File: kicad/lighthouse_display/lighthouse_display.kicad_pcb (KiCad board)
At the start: 2 copper layers, 132 x 66.4 mm, 134 parts, among them J1 Conn_01x12_Pin, U1 IS31FL3731-SA, U2 TPS61176RTER

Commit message: use 7*6 white LEDs in a row now, almost all leds connected
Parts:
- removed D107: 1206MIL, LED_SMD:LED_1206_3216Metric_Pad1.42x1.75mm_HandSolder
- R4: value 83k3 -> 68k
- moved D102 90.9 mm to (87.0, 98.1)
- moved D101 73.1 mm to (87.0, 105.0)
- moved D106 66.0 mm to (171.0, 77.2)
- moved D103 50.1 mm to (123.0, 98.1)
- moved D88 41.8 mm to (147.0, 63.7)
- moved D95 30.3 mm to (135.0, 105.0)
- moved D90 30.2 mm to (147.0, 70.2)
- moved D98 30.2 mm to (153.0, 94.4)
- moved D104 27.7 mm to (123.0, 84.1)
- moved D86 25.0 mm to (123.0, 70.2)
- moved D81 24.9 mm to (123.0, 91.1)
- moved D76 24.8 mm to (105.0, 94.3)
- moved D77 24.1 mm to (99.0, 98.1)
- moved D93 24.0 mm to (135.0, 98.1)
- moved D87 23.9 mm to (123.0, 77.2)
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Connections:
- D101 pad 1: unconnected-(D101-K-Pad1) -> WHLED1
- D101 pad 2: unconnected-(D101-A-Pad2) -> Net-(D101-A)
- D102 pad 1: unconnected-(D102-K-Pad1) -> WHLED2
- D102 pad 2: unconnected-(D102-A-Pad2) -> Net-(D102-A)
- D103 pad 1: unconnected-(D103-K-Pad1) -> WHLED3
- D103 pad 2: unconnected-(D103-A-Pad2) -> Net-(D103-A)
- D104 pad 1: unconnected-(D104-K-Pad1) -> WHLED4
- D104 pad 2: unconnected-(D104-A-Pad2) -> Net-(D104-A)
- D105 pad 1: unconnected-(D105-K-Pad1) -> WHLED5
- D105 pad 2: unconnected-(D105-A-Pad2) -> Net-(D105-A)
- D106 pad 1: unconnected-(D106-K-Pad1) -> WHLED6
- D106 pad 2: unconnected-(D106-A-Pad2) -> Net-(D106-A)
- D69 pad 1: WHLED1 -> Net-(D101-A)
- D75 pad 1: WHLED2 -> Net-(D102-A)
- D81 pad 1: WHLED3 -> Net-(D103-A)
- D87 pad 1: WHLED4 -> Net-(D104-A)
- D98 pad 1: WHLED5 -> Net-(D105-A)
- D99 pad 1: WHLED6 -> Net-(D106-A)
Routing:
- net VLEDWH: track 0.00 -> 49.2 mm
- net Net-(D95-K): track 0.00 -> 34.5 mm
- net Net-(D77-K): track 0.00 -> 23.7 mm
- net Net-(D79-K): track 0.00 -> 22.0 mm
- net WHLED6: track 0.00 -> 18.4 mm
- net WHLED2: track 0.00 -> 17.4 mm
- net Net-(D101-A): track 0.00 -> 17.4 mm
- net Net-(D89-K): track 0.00 -> 16.2 mm
- net Net-(D67-K): track 0.00 -> 15.8 mm
- net WHLED3: track 0.00 -> 12.6 mm
- net WHLED1: track 0.00 -> 12.4 mm
- net Net-(D80-K): track 0.00 -> 12.1 mm
- net Net-(D97-K): track 0.00 -> 10.7 mm
- net WHLED5: track 0.00 -> 10.4 mm
- net Net-(D96-K): track 0.00 -> 9.33 mm
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
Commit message: 100% routed
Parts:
- moved JP1 49.6 mm to (128.0, 114.9), turned to 180 degrees
- moved JP2 48.5 mm to (104.4, 114.9), turned to 180 degrees
- moved C2 11.3 mm to (162.6, 111.2), turned to 90 degrees
- moved C1 9.20 mm to (164.3, 111.1), turned to 90 degrees
- moved R4 4.30 mm to (160.1, 106.2)
- moved C5 3.22 mm to (160.6, 109.1), turned to -90 degrees
- moved C8 1.43 mm to (59.4, 102.4), turned to 90 degrees
- moved D100 1.05 mm to (163.6, 108.0)
- moved R3 1.01 mm to (163.4, 106.2), turned to 0 degrees
- moved C7 0.83 mm to (57.5, 102.2), turned to 90 degrees
- moved R11 0.05 mm to (73.4, 110.1)
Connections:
- U2 pad 17: (no net) -> GND
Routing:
- net VLEDWH: track 49.2 -> 207.8 mm, vias 0 -> 7
- net /WHITE_PWM: track 0.00 -> 82.8 mm, vias 0 -> 5
- net WHLED1: track 12.4 -> 85.6 mm
- net WHLED2: track 17.4 -> 88.2 mm
- net /~{SDB}: track 3.36 -> 72.1 mm, vias 0 -> 2
- net /~{INTB}: track 1.90 -> 67.9 mm, vias 0 -> 2
- net +3.3V: track 9.66 -> 74.2 mm, vias 0 -> 2
- net /TPS_VIN: track 0.00 -> 59.4 mm
- net WHLED4: track 3.83 -> 60.6 mm, vias 0 -> 2
- net /IS_VIN: track 8.61 -> 64.5 mm
- net /SCL: track 4.04 -> 58.6 mm, vias 1 -> 4
- net /SDA: track 4.38 -> 58.6 mm, vias 1 -> 4
- net CB1: track 178.0 -> 224.9 mm, vias 5 -> 6
- net +12V: track 0.00 -> 46.9 mm
- net CB2: track 186.0 -> 232.7 mm, vias 5 -> 6
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- added copper zone on B.Cu, net GND
- added copper zone on F.Cu, net GND

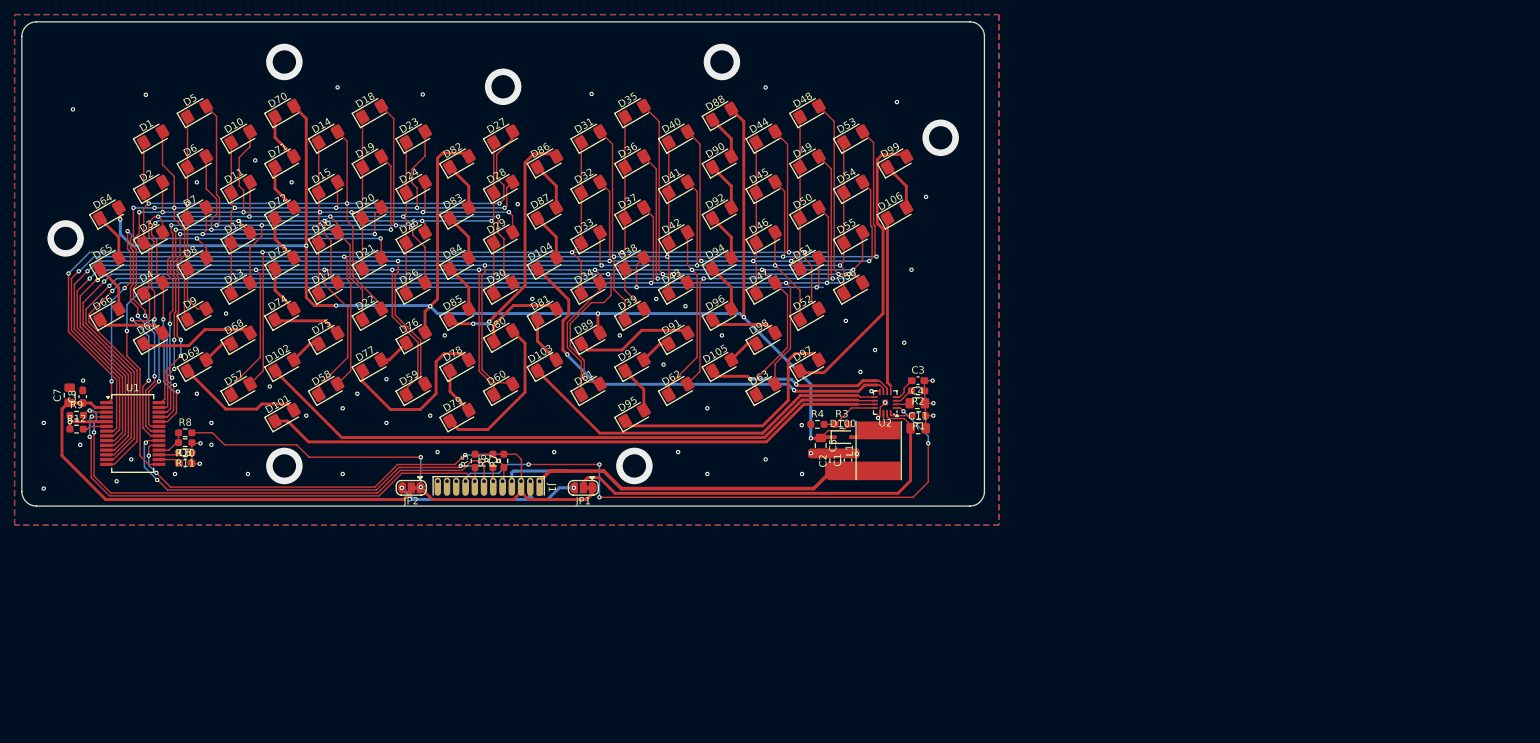
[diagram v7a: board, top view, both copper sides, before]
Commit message: started with button pcb
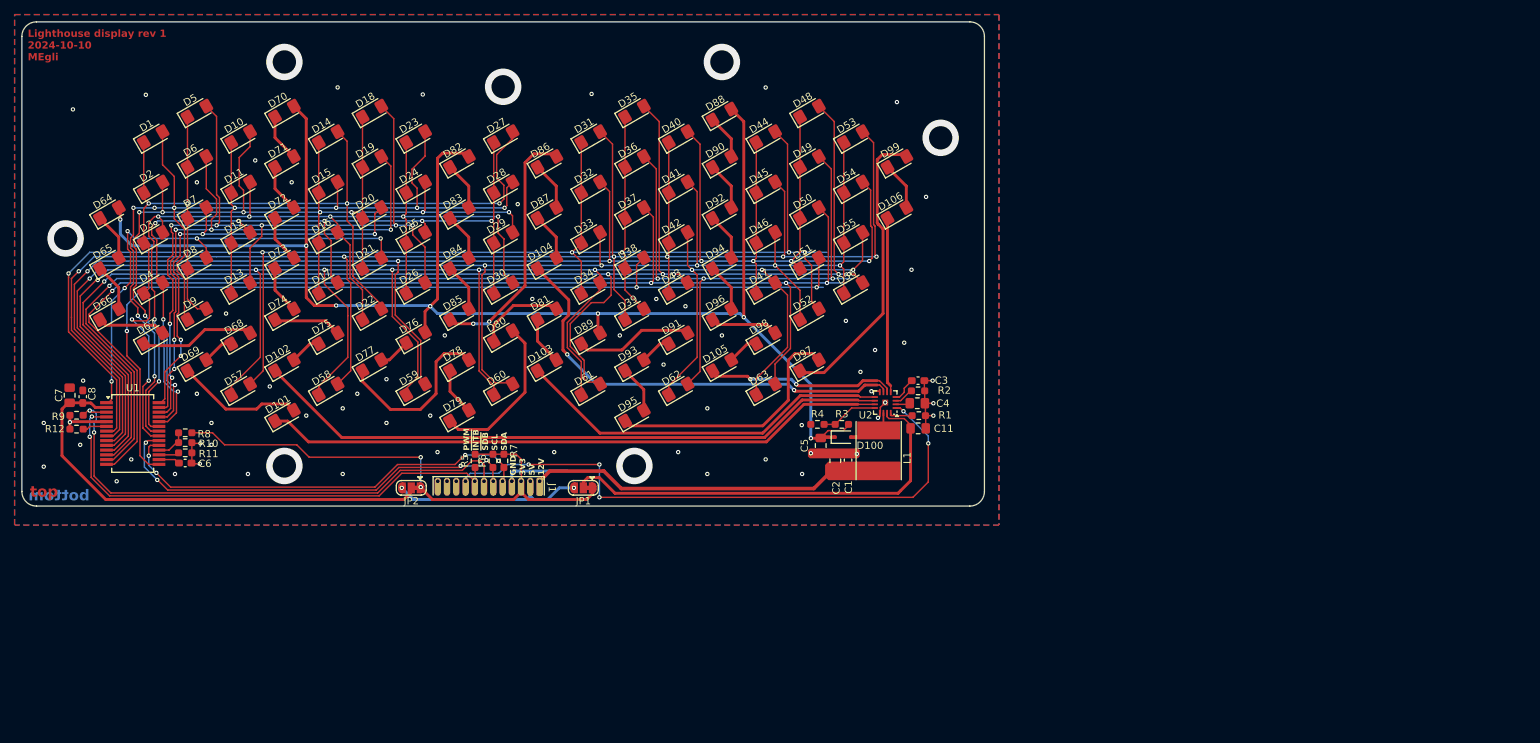
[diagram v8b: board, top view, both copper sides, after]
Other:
- board text added: "GND 3V3 5V 12V"
- board text added: "Lighthouse display rev 1 2024-10-10 MEgli"
- board text added: "PWM ~{INTB} ~{SDB} SCL SDA"
- board text added: "bottom"
- board text added: "top"
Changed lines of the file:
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@@
 		(tags "resistor handsolder")
 		(property "Reference" "R8"
-			(at 0 -1.43 0)
+			(at 2.6 0.17 0)
 			(layer "F.SilkS")
 			(effects
@@
 		(tags "net tie solder jumper bridged")
 		(property "Reference" "JP1"
-			(at 0 -1.8 360)
+			(at 0 -1.8 0)
 			(layer "F.SilkS")
 			(effects
@@
 		)
 		(property "Value" "Jumper_3_Bridged12"
-			(at 0 1.9 360)
+			(at 0 1.9 0)
 			(layer "F.Fab")
 			(effects
@@
 		(tags "resistor handsolder")
 		(property "Reference" "R7"
-			(at 0 -1.43 90)
+			(at 1.4 1.37 90)
 			(layer "F.SilkS")
 			(effects
@@
 		(tags "capacitor handsolder")
 		(property "Reference" "C11"
-			(at 0 -1.68 0)
+			(at 3.5 0.02 0)
 			(layer "F.SilkS")
 			(effects
@@
 		(tags "capacitor handsolder")
 		(property "Reference" "C4"
-			(at 0 -1.68 0)
+			(at 3.5 0.02 0)
 			(layer "F.SilkS")
 			(effects
@@
 		(tags "resistor handsolder")
 		(property "Reference" "R11"
-			(at 0 -1.43 0)
+			(at -3.2 -0.13 0)
 			(layer "F.SilkS")
 			(effects
@@
 		(tags "resistor handsolder")
 		(property "Reference" "R12"
-			(at 0 -1.43 0)
+			(at -3 -0.03 0)
 			(layer "F.SilkS")
 			(effects
@@
 		(tags "resistor handsolder")
 		(property "Reference" "R1"
-			(at 0 -1.43 0)
+			(at -3.6 0.07 0)
 			(layer "F.SilkS")
 			(effects
@@
 		(tags "resistor handsolder")
 		(property "Reference" "R2"
-			(at 0 -1.43 0)
+			(at -3.6 0.07 0)
 			(layer "F.SilkS")
 			(effects
@@
 		(tags "capacitor handsolder")
 		(property "Reference" "C5"
-			(at 0 -1.68 90)
+			(at 0 2.22 90)
 			(layer "F.SilkS")
 			(effects
@@
 		(tags "resistor handsolder")
 		(property "Reference" "R3"
-			(at 0 -1.43 360)
+			(at 0 -1.43 0)
 			(layer "F.SilkS")
 			(effects
@@
 		)
 		(property "Value" "1M"
-			(at 0 1.43 360)
+			(at 0 1.43 0)
 			(layer "F.Fab")
 			(effects
@@
 		)
 		(fp_text user "${REFERENCE}"
-			(at 0 0 360)
+			(at 0 0 0)
 			(layer "F.Fab")
 			(effects
@@
 		(tags "capacitor handsolder")
 		(property "Reference" "C6"
-			(at 0 -1.43 0)
+			(at 2.7 0.07 0)
 			(layer "F.SilkS")
 			(effects
@@
 		(tags "capacitor handsolder")
 		(property "Reference" "C2"
-			(at 0 -1.68 90)
+			(at -3.7 0.12 90)
 			(layer "F.SilkS")
 			(effects
@@
 		(tags "resistor handsolder")
 		(property "Reference" "R10"
-			(at 0 -1.43 0)
+			(at -3.2 -0.13 0)
 			(layer "F.SilkS")
 			(effects
@@
 		(tags "inductor taiyo-yuden nr smd")
 		(property "Reference" "L1"
-			(at 0 -4 90)
+			(at -1 3.9 90)
 			(layer "F.SilkS")
 			(effects
@@
 		(tags "SOD-323F")
 		(property "Reference" "D100"
-			(at 0 -1.85 0)
+			(at 3.7 1.15 0)
 			(layer "F.SilkS")
 			(effects
@@
 		(tags "Texas WQFN NoLead")
 		(property "Reference" "U2"
-			(at 0 -2.83 0)
+			(at 2.7 -1.73 0)
 			(layer "F.SilkS")
 			(effects
@@
 		(tags "resistor handsolder")
 		(property "Reference" "R4"
-			(at 0 -1.43 360)
+			(at 0 -1.43 0)
 			(layer "F.SilkS")
 			(effects
@@
 		)
 		(property "Value" "68k"
-			(at 0 1.43 360)
+			(at 0 1.43 0)
 			(layer "F.Fab")
 			(effects
@@
 		)
 		(fp_text user "${REFERENCE}"
-			(at 0 0 360)
+			(at 0 0 0)
 			(layer "F.Fab")
 			(effects
@@
 		(tags "capacitor handsolder")
 		(property "Reference" "C8"
-			(at 0 -1.43 90)
+			(at 0.4 1.27 90)
 			(layer "F.SilkS")
 			(effects
@@
 		(tags "resistor handsolder")
 		(property "Reference" "R9"
-			(at 0 -1.43 0)
+			(at -2.5 0.17 0)
 			(layer "F.SilkS")
 			(effects
@@
 		(tags "capacitor handsolder")
 		(property "Reference" "C7"
-			(at 0 -1.68 90)
+			(at 0 -1.48 90)
 			(layer "F.SilkS")
 			(effects
@@
 		(tags "net tie solder jumper bridged")
 		(property "Reference" "JP2"
-			(at 0 -1.8 360)
+			(at 0 -1.8 0)
 			(layer "F.SilkS")
 			(effects
@@
 		)
 		(property "Value" "Jumper_3_Bridged12"
-			(at 0 1.9 360)
+			(at 0 1.9 0)
 			(layer "F.Fab")
 			(effects
@@
 		(tags "capacitor handsolder")
 		(property "Reference" "C1"
-			(at 0 -1.43 90)
+			(at -3.7 0.07 90)
 			(layer "F.SilkS")
 			(effects
@@
 		(tags "capacitor handsolder")
 		(property "Reference" "C3"
-			(at 0 -1.43 0)
+			(at 3.2 -0.03 0)
 			(layer "F.SilkS")
 			(effects
@@
 		(layer "Edge.Cuts")
 	)
+	(gr_text "Lighthouse display rev 1\n2024-10-10\nMEgli"
+		(at 51.8 56.4 0)
+		(layer "F.Cu")
+		(effects
+			(font
+				(size 1 1)
+				(thickness 0.2)
+				(bold yes)
+			)
+			(justify left bottom)
+		)
+	)
+	(gr_text "top"
+		(at 52.1 116.3 0)
+		(layer "F.Cu")
+		(effects
+			(font
+				(size 1.5 1.5)
+				(thickness 0.3)
+				(bold yes)
+			)
+			(justify left bottom)
+		)
+	)
+	(gr_text "bottom"
+		(at 60.3 116.8 0)
+		(layer "B.Cu")
+		(effects
+			(font
+				(size 1.5 1.5)
+				(thickness 0.3)
+				(bold yes)
+			)
+			(justify left bottom mirror)
+		)
+	)
+	(gr_text "PWM\n~{INTB}\n~{SDB}\nSCL\nSDA"
+		(at 117.6 109.8 90)
+		(layer "F.SilkS")
+		(effects
+			(font
+				(size 0.8 0.8)
+				(thickness 0.2)
+				(bold yes)
+			)
+			(justify left bottom)
+		)
+	)
+	(gr_text "GND\n3V3\n5V\n12V"
+		(at 122.7 113.2 90)
+		(layer "F.SilkS")
+		(effects
+			(font
+				(size 0.8 0.8)
+				(thickness 0.2)
+				(bold yes)
+			)
+			(justify left bottom)
+		)
+	)
 	(dimension
 		(type aligned)
@@
 	)
 	(via
-		(at 54 115)
+		(at 54 112)
 		(size 0.6)
 		(drill 0.3)
